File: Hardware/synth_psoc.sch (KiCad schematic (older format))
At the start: 0 parts

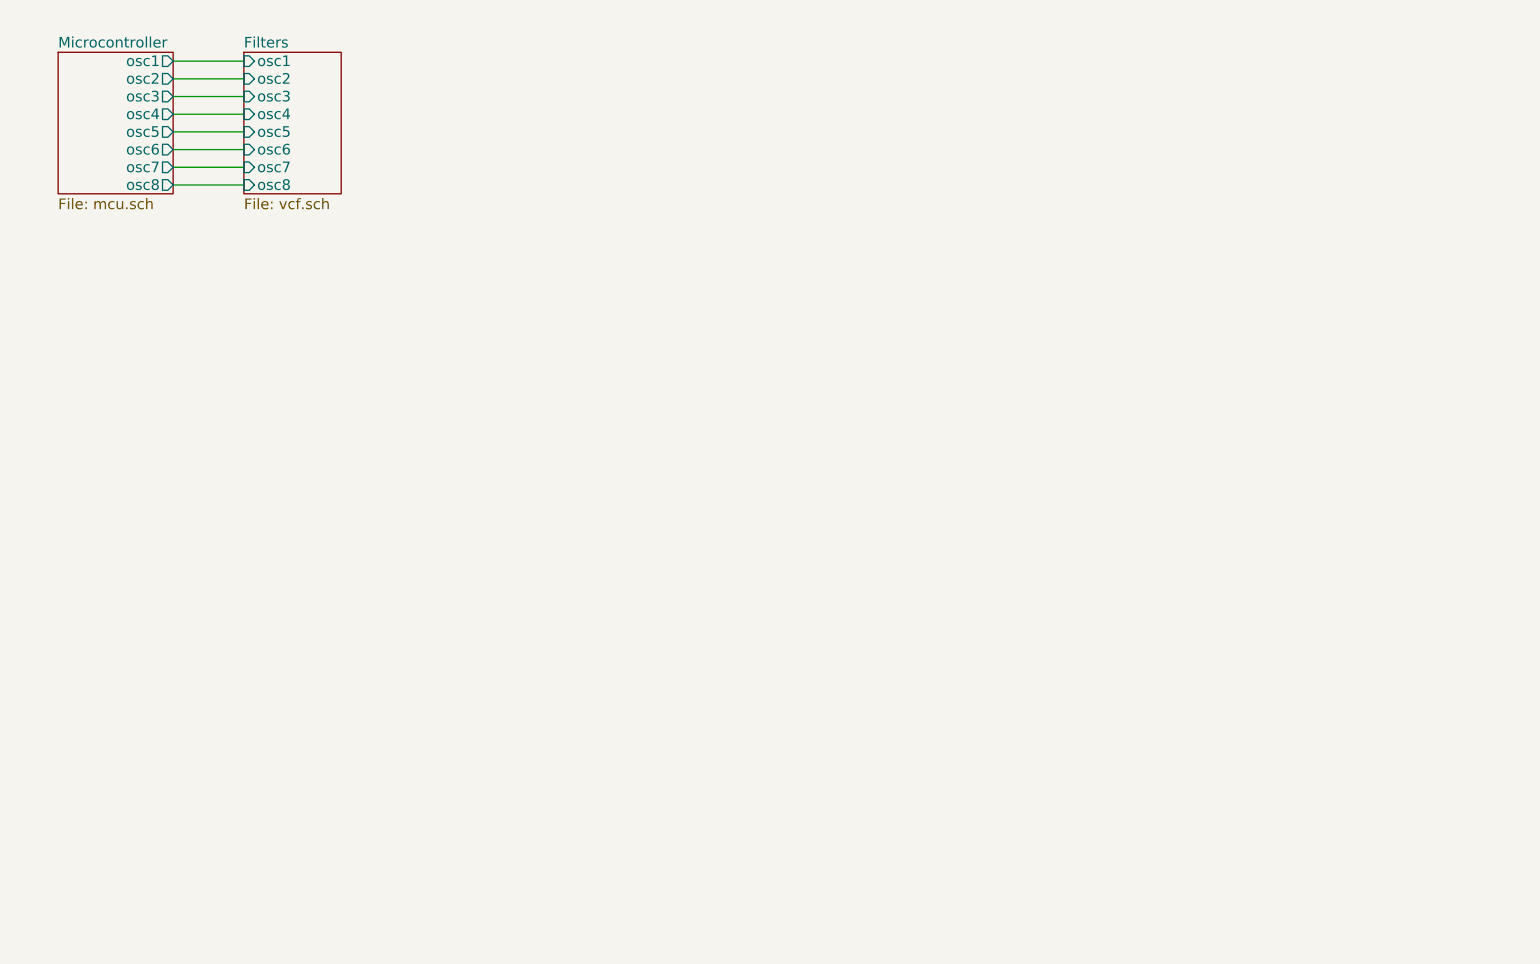
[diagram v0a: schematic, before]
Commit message: add sheets for the remaining functionality. This should hopefully be all sheets, but might add more if necessary.
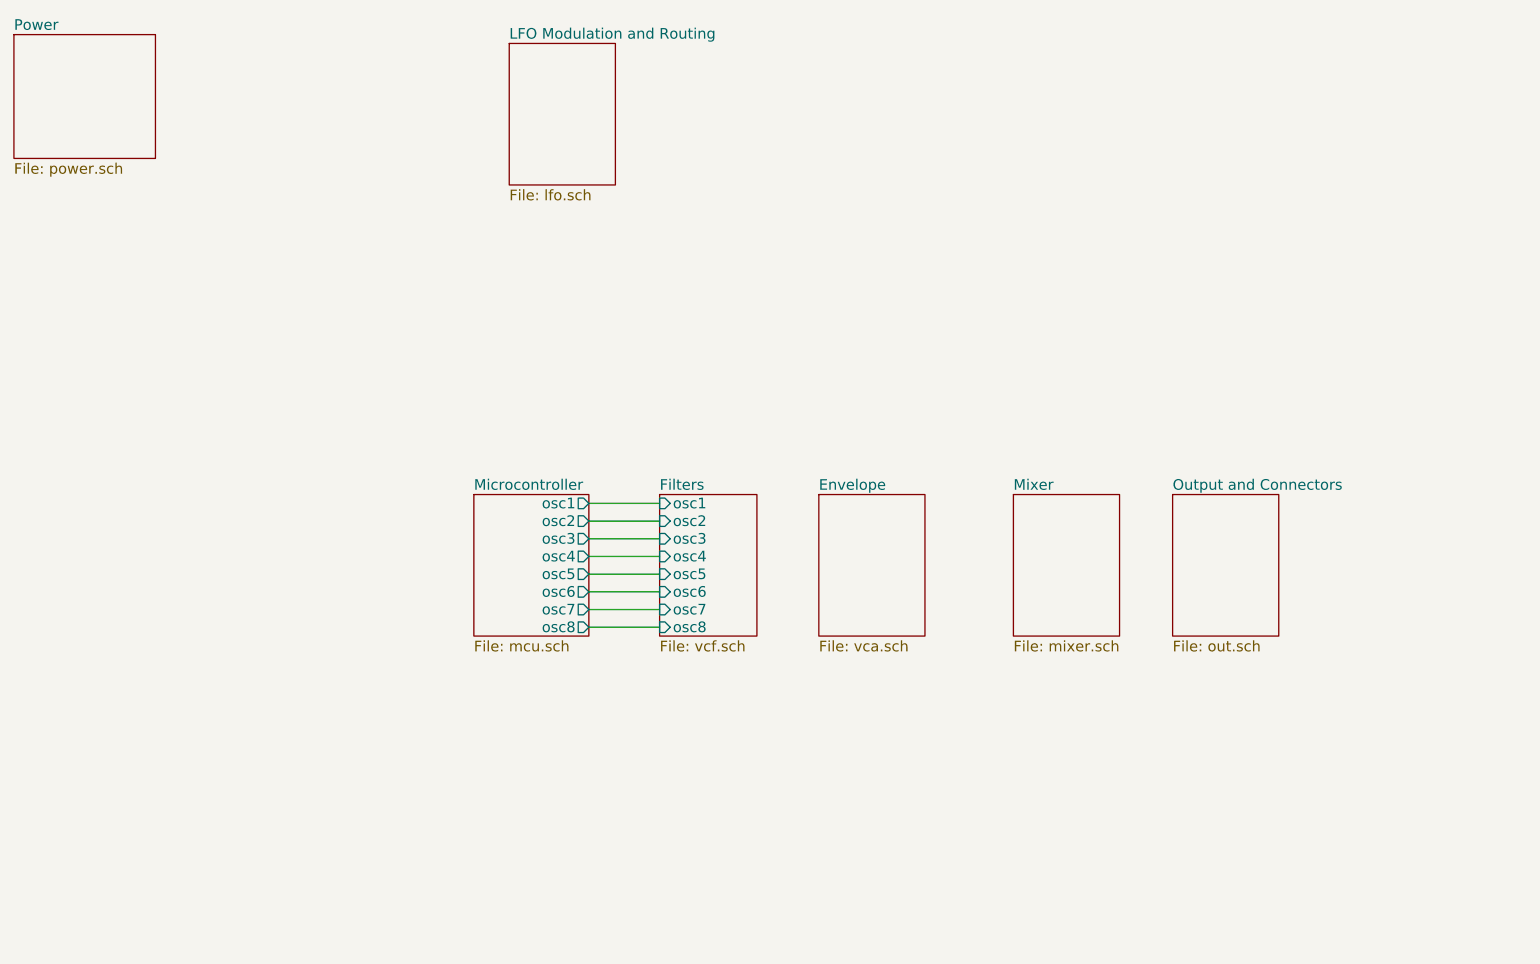
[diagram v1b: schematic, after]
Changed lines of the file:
@@
 $Descr A4 11693 8268
 encoding utf-8
-Sheet 1 3
+Sheet 1 7
 Title ""
 Date ""
@@
 $EndDescr
 $Sheet
-S 900  750  650  800
+S 3250 3250 650  800
 U 5C3546FC
 F0 "Microcontroller" 60
 F1 "mcu.sch" 60
-F2 "osc1" O R 1550 800 60
-F3 "osc2" O R 1550 900 60
-F4 "osc3" O R 1550 1000 60
-F5 "osc4" O R 1550 1100 60
-F6 "osc5" O R 1550 1200 60
-F7 "osc6" O R 1550 1300 60
-F8 "osc7" O R 1550 1400 60
-F9 "osc8" O R 1550 1500 60
+F2 "osc1" O R 3900 3300 60
+F3 "osc2" O R 3900 3400 60
+F4 "osc3" O R 3900 3500 60
+F5 "osc4" O R 3900 3600 60
+F6 "osc5" O R 3900 3700 60
+F7 "osc6" O R 3900 3800 60
+F8 "osc7" O R 3900 3900 60
+F9 "osc8" O R 3900 4000 60
 $EndSheet
 $Sheet
-S 1950 750  550  800
+S 4300 3250 550  800
 U 5C355489
 F0 "Filters" 60
 F1 "vcf.sch" 60
-F2 "osc1" I L 1950 800 60
-F3 "osc2" I L 1950 900 60
-F4 "osc3" I L 1950 1000 60
-F5 "osc4" I L 1950 1100 60
-F6 "osc5" I L 1950 1200 60
-F7 "osc6" I L 1950 1300 60
-F8 "osc7" I L 1950 1400 60
-F9 "osc8" I L 1950 1500 60
+F2 "osc1" I L 4300 3300 60
+F3 "osc2" I L 4300 3400 60
+F4 "osc3" I L 4300 3500 60
+F5 "osc4" I L 4300 3600 60
+F6 "osc5" I L 4300 3700 60
+F7 "osc6" I L 4300 3800 60
+F8 "osc7" I L 4300 3900 60
+F9 "osc8" I L 4300 4000 60
 $EndSheet
 Wire Wire Line
-	1550 800  1950 800
+	3900 3300 4300 3300
 Wire Wire Line
-	1550 900  1950 900
+	3900 3400 4300 3400
 Wire Wire Line
-	1550 1000 1950 1000
+	3900 3500 4300 3500
 Wire Wire Line
-	1550 1100 1950 1100
+	3900 3600 4300 3600
 Wire Wire Line
-	1550 1200 1950 1200
+	3900 3700 4300 3700
 Wire Wire Line
-	1550 1300 1950 1300
+	3900 3800 4300 3800
 Wire Wire Line
-	1550 1400 1950 1400
+	3900 3900 4300 3900
 Wire Wire Line
-	1550 1500 1950 1500
+	3900 4000 4300 4000
+$Sheet
+S 650  650  800  700
+U 5C356C07
+F0 "Power" 60
+F1 "power.sch" 60
+$EndSheet
+$Sheet
+S 5200 3250 600  800
+U 5C356D9E
+F0 "Envelope" 60
+F1 "vca.sch" 60
+$EndSheet
+$Sheet
+S 6300 3250 600  800
+U 5C357081
+F0 "Mixer" 60
+F1 "mixer.sch" 60
+$EndSheet
+$Sheet
+S 3450 700  600  800
+U 5C35738C
+F0 "LFO Modulation and Routing" 60
+F1 "lfo.sch" 60
+$EndSheet
+$Sheet
+S 7200 3250 600  800
+U 5C357E40
+F0 "Output and Connectors" 60
+F1 "out.sch" 60
+$EndSheet
 $EndSCHEMATC

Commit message: add basic version of VCA for one channel
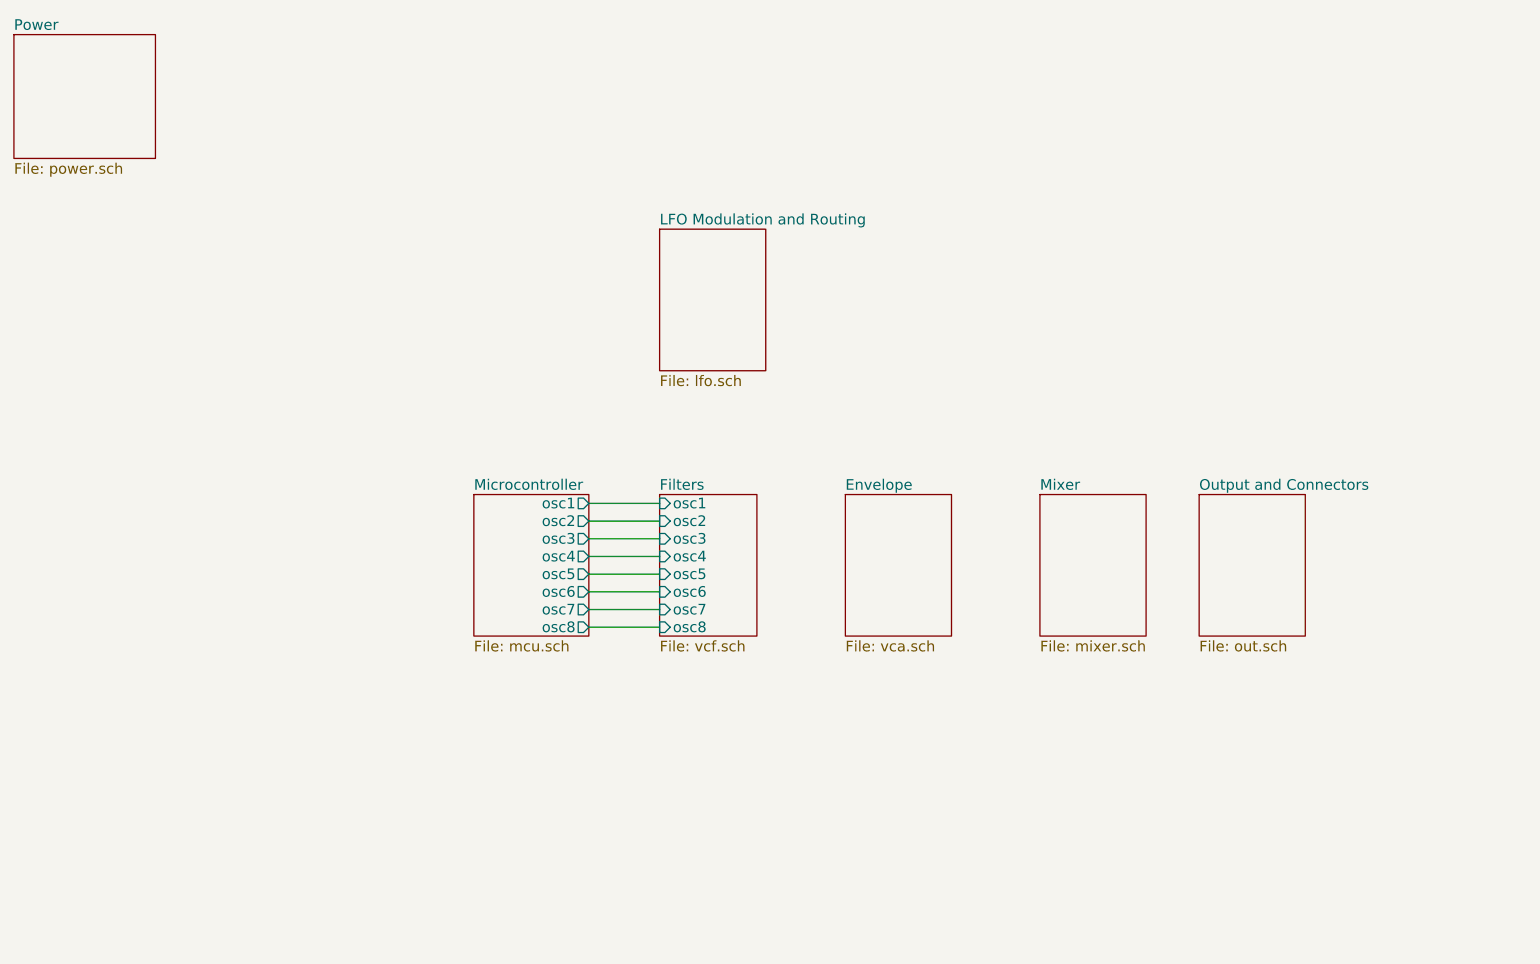
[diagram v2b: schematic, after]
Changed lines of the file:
@@
 $Descr A4 11693 8268
 encoding utf-8
-Sheet 1 7
+Sheet 1 8
 Title ""
 Date ""
@@
 $EndSheet
 $Sheet
-S 5200 3250 600  800
+S 5350 3250 600  800
 U 5C356D9E
 F0 "Envelope" 60
@@
 $EndSheet
 $Sheet
-S 6300 3250 600  800
+S 6450 3250 600  800
 U 5C357081
 F0 "Mixer" 60
@@
 $EndSheet
 $Sheet
-S 3450 700  600  800
+S 4300 1750 600  800
 U 5C35738C
 F0 "LFO Modulation and Routing" 60
@@
 $EndSheet
 $Sheet
-S 7200 3250 600  800
+S 7350 3250 600  800
 U 5C357E40
 F0 "Output and Connectors" 60

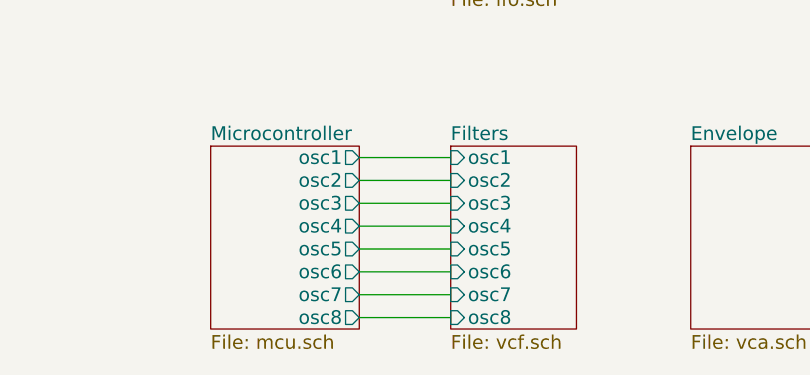
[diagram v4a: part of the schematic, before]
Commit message: connect frequency potentiometers to mcu
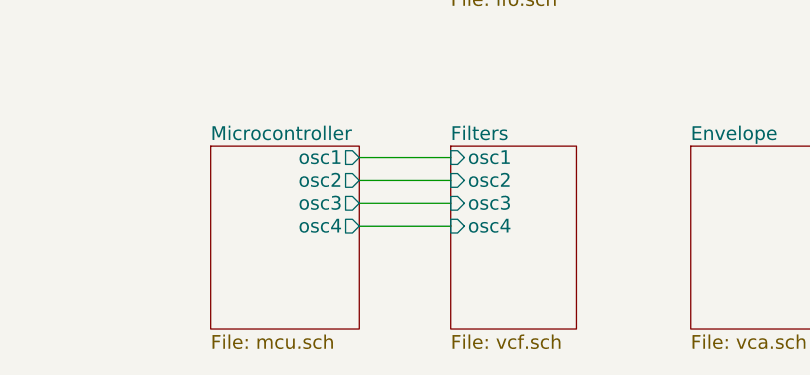
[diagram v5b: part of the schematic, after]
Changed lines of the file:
@@
 F4 "osc3" O R 3900 3500 60
 F5 "osc4" O R 3900 3600 60
-F6 "osc5" O R 3900 3700 60
-F7 "osc6" O R 3900 3800 60
-F8 "osc7" O R 3900 3900 60
-F9 "osc8" O R 3900 4000 60
 $EndSheet
 $Sheet
@@
 F4 "osc3" I L 4300 3500 60
 F5 "osc4" I L 4300 3600 60
-F6 "osc5" I L 4300 3700 60
-F7 "osc6" I L 4300 3800 60
-F8 "osc7" I L 4300 3900 60
-F9 "osc8" I L 4300 4000 60
 $EndSheet
 Wire Wire Line
@@
 Wire Wire Line
 	3900 3600 4300 3600
-Wire Wire Line
-	3900 3700 4300 3700
-Wire Wire Line
-	3900 3800 4300 3800
-Wire Wire Line
-	3900 3900 4300 3900
-Wire Wire Line
-	3900 4000 4300 4000
 $Sheet
 S 650  650  800  700
